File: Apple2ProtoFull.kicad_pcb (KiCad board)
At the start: 2 copper layers, 254 x 76.4 mm, 3 parts, among them J1 Apple II Bus Card Edge, J2 Apple II Bus Card Pin Header

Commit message: Added Midsized 7" board. Found spec on Apple II Expansion Card sizes (adding to repo). Updated all boards to be within spec (mostly).
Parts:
- moved J1 0.31 mm to (196.5, 136.7)
- moved J2 0.31 mm to (196.5, 124.4)
- moved REF** 0.31 mm to (176.2, 128.2)
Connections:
- net /NC/Col renamed /NC/Color
- J1 pad 38: /Phi0 -> /Phi1
- J1 pad 40: /Phi1 -> /Phi0
- J2 pad 38: /Phi0 -> /Phi1
- J2 pad 40: /Phi1 -> /Phi0
- REF** pad : (no net) -> /Phi0
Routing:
- net +5V: track 658.7 -> 546.9 mm
- net GND: track 663.5 -> 570.7 mm
- net /~{DEVICE_SELECT}: track 15.9 -> 24.7 mm
- net /Phi1: track 15.9 -> 24.7 mm
- net /DMA_IN: track 15.9 -> 24.7 mm
- net +12V: track 372.9 -> 381.8 mm
- net /Q3: track 15.9 -> 24.7 mm
- net /D05: track 15.9 -> 24.7 mm
- net /NC/Color: track 15.9 -> 24.7 mm
- net /D06: track 15.9 -> 24.7 mm
- net /D00: track 15.9 -> 24.7 mm
- net /7M: track 15.9 -> 24.7 mm
- net /~{RES}: track 15.9 -> 24.7 mm
- net /~{IRQ}: track 15.9 -> 24.7 mm
- net /USER_1: track 15.9 -> 24.7 mm
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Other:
- outline, holes or cut-outs redrawn
- board text added: "NC/Color"
- board text removed: "NC/COL"

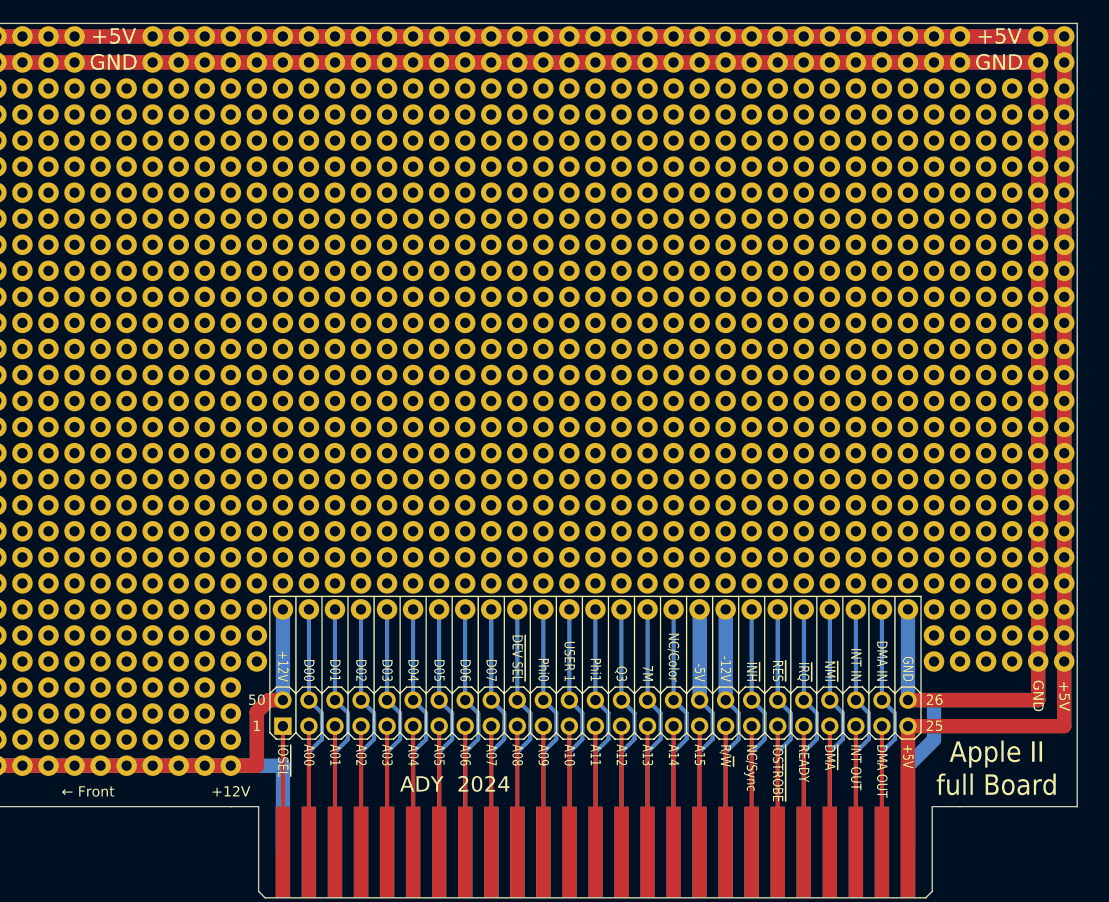
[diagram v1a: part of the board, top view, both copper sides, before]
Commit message: Updated Silk Screen to be easier to read. Added more Apple II documentation.
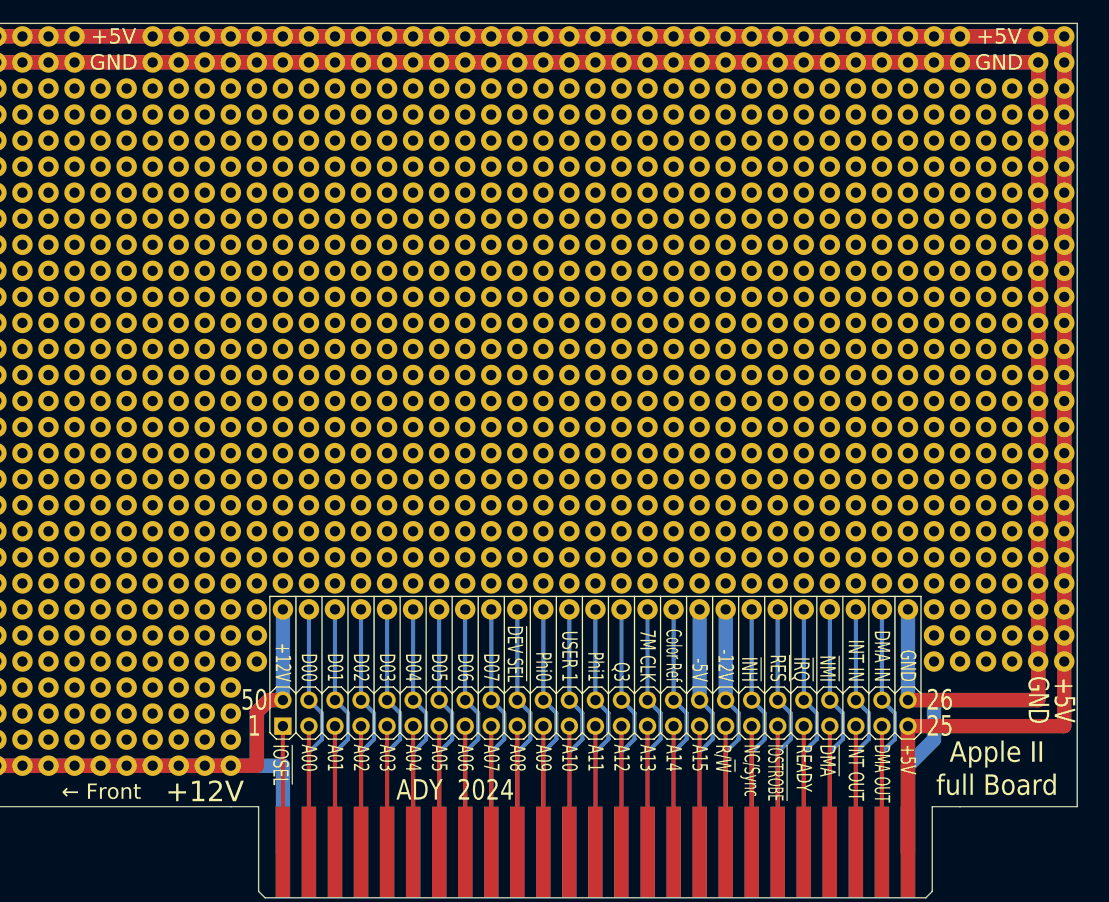
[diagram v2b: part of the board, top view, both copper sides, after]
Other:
- board text added: "7M CLK"
- board text added: "Color Ref"
- board text removed: "7M"
- board text removed: "NC/Color"
